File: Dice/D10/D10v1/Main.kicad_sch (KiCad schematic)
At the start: 27 parts, among them J1 Conn_01x14, J2 Conn_01x11, U1 N52810_QFN32, U2 KXTJ3-1057, Y1 32MHz 40ppm

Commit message: More Cleanup of Dice Boards
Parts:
- C2, C5: value 6pF 10V 10% -> 8pF 10V 10%; Manufacturer Murata -> (none); Manufacturer Part Number GCM1555C1H6R0DA16D -> (none)
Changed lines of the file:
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@@
     (in_bom yes) (on_board yes)
     (property "Reference" "C2" (id 0) (at 173.99 39.3192 90))
-    (property "Value" "6pF 10V 10%" (id 1) (at 173.99 41.6306 90))
+    (property "Value" "8pF 10V 10%" (id 1) (at 173.99 41.6306 90))
     (property "Footprint" "Capacitor_SMD:C_0402_1005Metric" (id 2) (at 170.18 46.6852 0)
       (effects (font (size 1.27 1.27)) hide)
@@
       (effects (font (size 1.27 1.27)) hide)
     )
-    (property "Manufacturer" "Murata" (id 6) (at 173.99 45.72 0)
-      (effects (font (size 1.27 1.27)) hide)
-    )
-    (property "Manufacturer Part Number" "GCM1555C1H6R0DA16D" (id 7) (at 173.99 45.72 0)
+    (property "Manufacturer" "" (id 6) (at 173.99 45.72 0)
+      (effects (font (size 1.27 1.27)) hide)
+    )
+    (property "Manufacturer Part Number" "" (id 7) (at 173.99 45.72 0)
       (effects (font (size 1.27 1.27)) hide)
     )
@@
     (in_bom yes) (on_board yes)
     (property "Reference" "C5" (id 0) (at 173.99 54.61 90))
-    (property "Value" "6pF 10V 10%" (id 1) (at 173.99 62.23 90))
+    (property "Value" "8pF 10V 10%" (id 1) (at 173.99 62.23 90))
     (property "Footprint" "Capacitor_SMD:C_0402_1005Metric" (id 2) (at 170.18 59.3852 0)
       (effects (font (size 1.27 1.27)) hide)
@@
       (effects (font (size 1.27 1.27)) hide)
     )
-    (property "Manufacturer" "Murata" (id 6) (at 173.99 58.42 0)
-      (effects (font (size 1.27 1.27)) hide)
-    )
-    (property "Manufacturer Part Number" "GCM1555C1H6R0DA16D" (id 7) (at 173.99 58.42 0)
+    (property "Manufacturer" "" (id 6) (at 173.99 58.42 0)
+      (effects (font (size 1.27 1.27)) hide)
+    )
+    (property "Manufacturer Part Number" "" (id 7) (at 173.99 58.42 0)
       (effects (font (size 1.27 1.27)) hide)
     )
@@
     )
     (path "/00000000-0000-0000-0000-00005b9e93ff"
-      (reference "C2") (unit 1) (value "6pF 10V 10%") (footprint "Capacitor_SMD:C_0402_1005Metric")
+      (reference "C2") (unit 1) (value "8pF 10V 10%") (footprint "Capacitor_SMD:C_0402_1005Metric")
     )
     (path "/00000000-0000-0000-0000-00005b9e68c9"
@@
     )
     (path "/00000000-0000-0000-0000-00005b9e9491"
-      (reference "C5") (unit 1) (value "6pF 10V 10%") (footprint "Capacitor_SMD:C_0402_1005Metric")
+      (reference "C5") (unit 1) (value "8pF 10V 10%") (footprint "Capacitor_SMD:C_0402_1005Metric")
     )
     (path "/00000000-0000-0000-0000-00005bb44a54/00000000-0000-0000-0000-00005e5dc7cc"

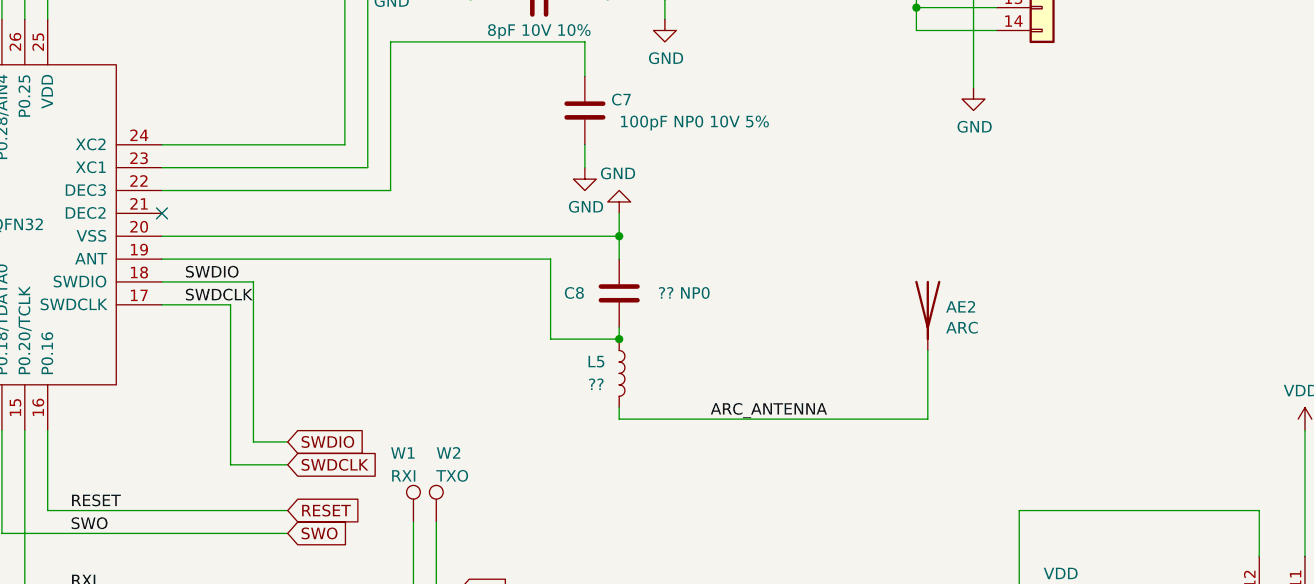
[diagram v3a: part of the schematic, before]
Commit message: Updating D8 and D10 boards, new antenna, etc...
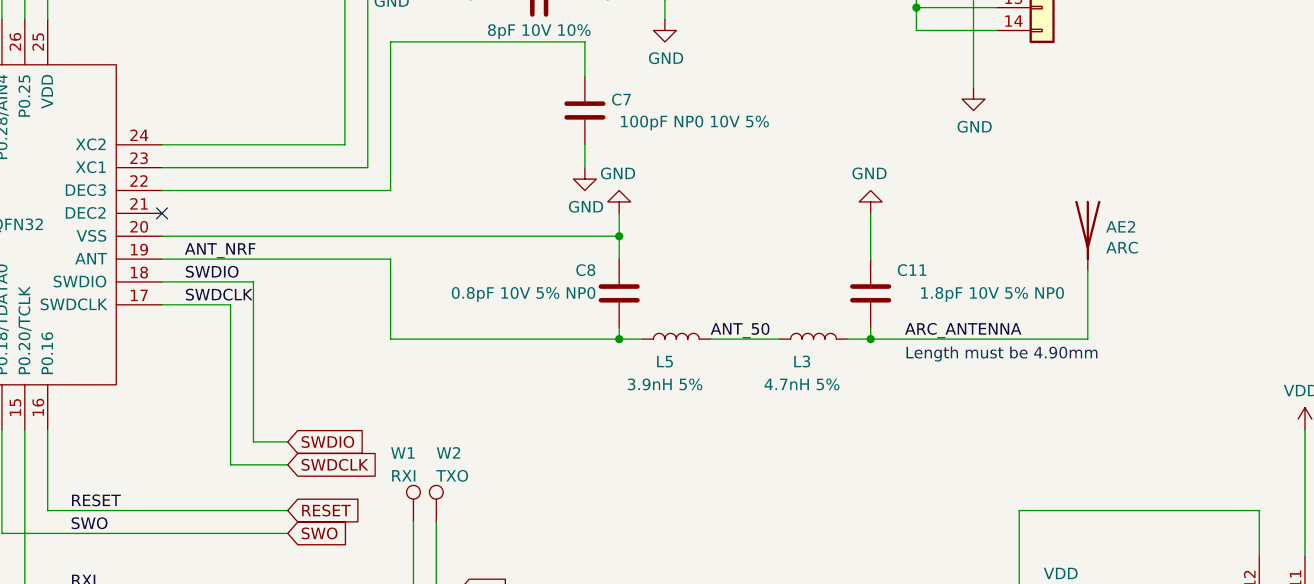
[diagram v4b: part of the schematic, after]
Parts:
- added C11: 1.8pF 10V 5% NP0, Pixels-dice:0402_RF, symbol Device:C
- added L3: 4.7nH 5%, Pixels-dice:0402_RF, symbol Device:L
- AE2: Generic OK (none) -> N/A; Manufacturer (none) -> AEM Antennas
- C2, C5: Manufacturer (none) -> Murata; Manufacturer Part Number (none) -> GRM1555C2A8R0DA01D
- C8: value ?? NP0 -> 0.8pF 10V 5% NP0; footprint Capacitor_SMD:C_0402_1005Metric -> Pixels-dice:0402_RF; Manufacturer (none) -> Murata; Manufacturer Part Number (none) -> GCM1555C1HR80BA16D
- J1, J2, W1, W2, W5, W7, W8, W9: Generic OK (none) -> N/A
- L5: value ?? -> 3.9nH 5%; footprint Inductor_SMD:L_0402_1005Metric -> Pixels-dice:0402_RF; Manufacturer (none) -> Murata; Manufacturer Part Number (none) -> LQG15HS3N9B02D
- R9: Manufacturer (none) -> Yageo; Manufacturer Part Number (none) -> AC0402FR-07270KL
- U2: Generic OK (none) -> NO
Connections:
- net ARC_ANTENNA: now also C11.1, L3.2; no longer L5.2
- net GND: now also C11.2
- net ANT_NRF: now reaches C8.1, L5.1, U1.19 (ANT)
- new net ANT_50: L3.1, L5.2
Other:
- note added: "Length must be 4.90mm"
